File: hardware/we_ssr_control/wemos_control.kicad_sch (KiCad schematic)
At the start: 17 parts, among them U1 WeMos_D1_mini

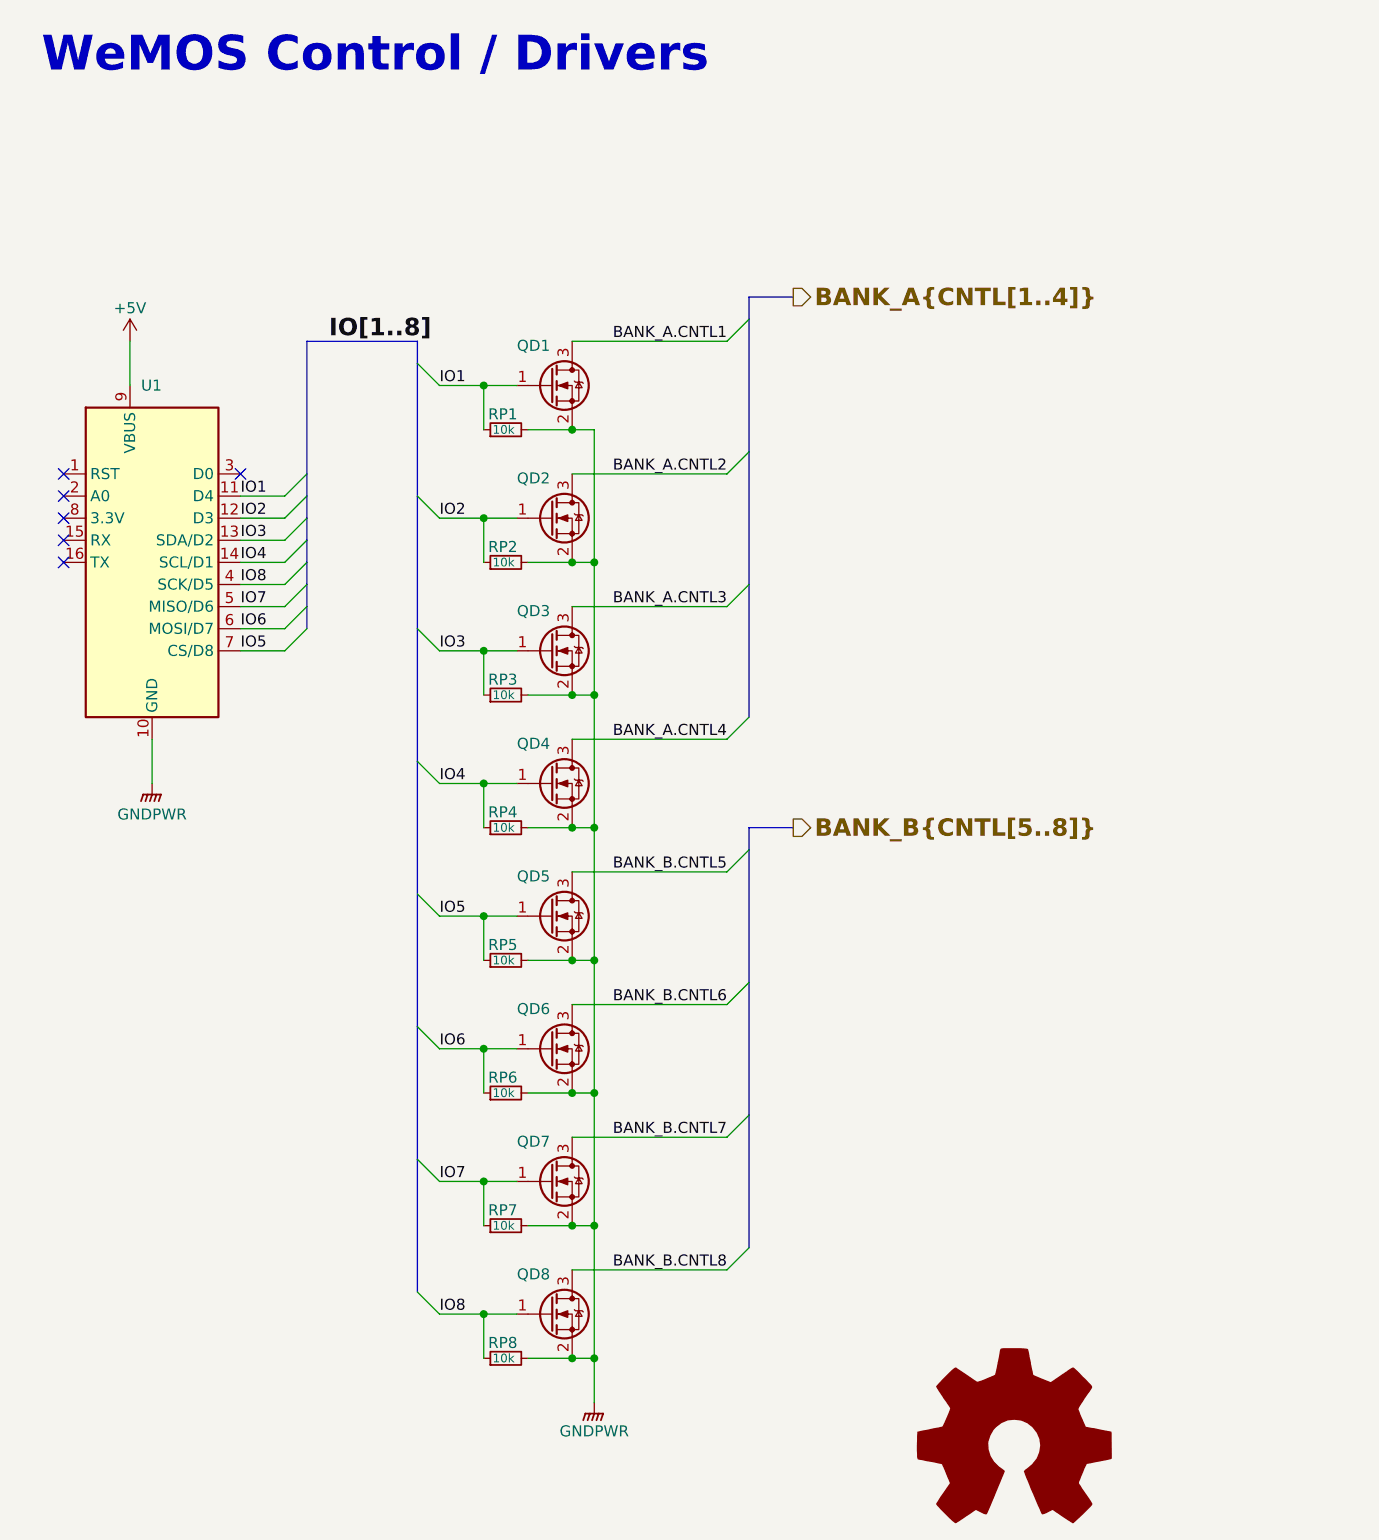
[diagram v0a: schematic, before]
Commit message: Power supply changes plus misc.
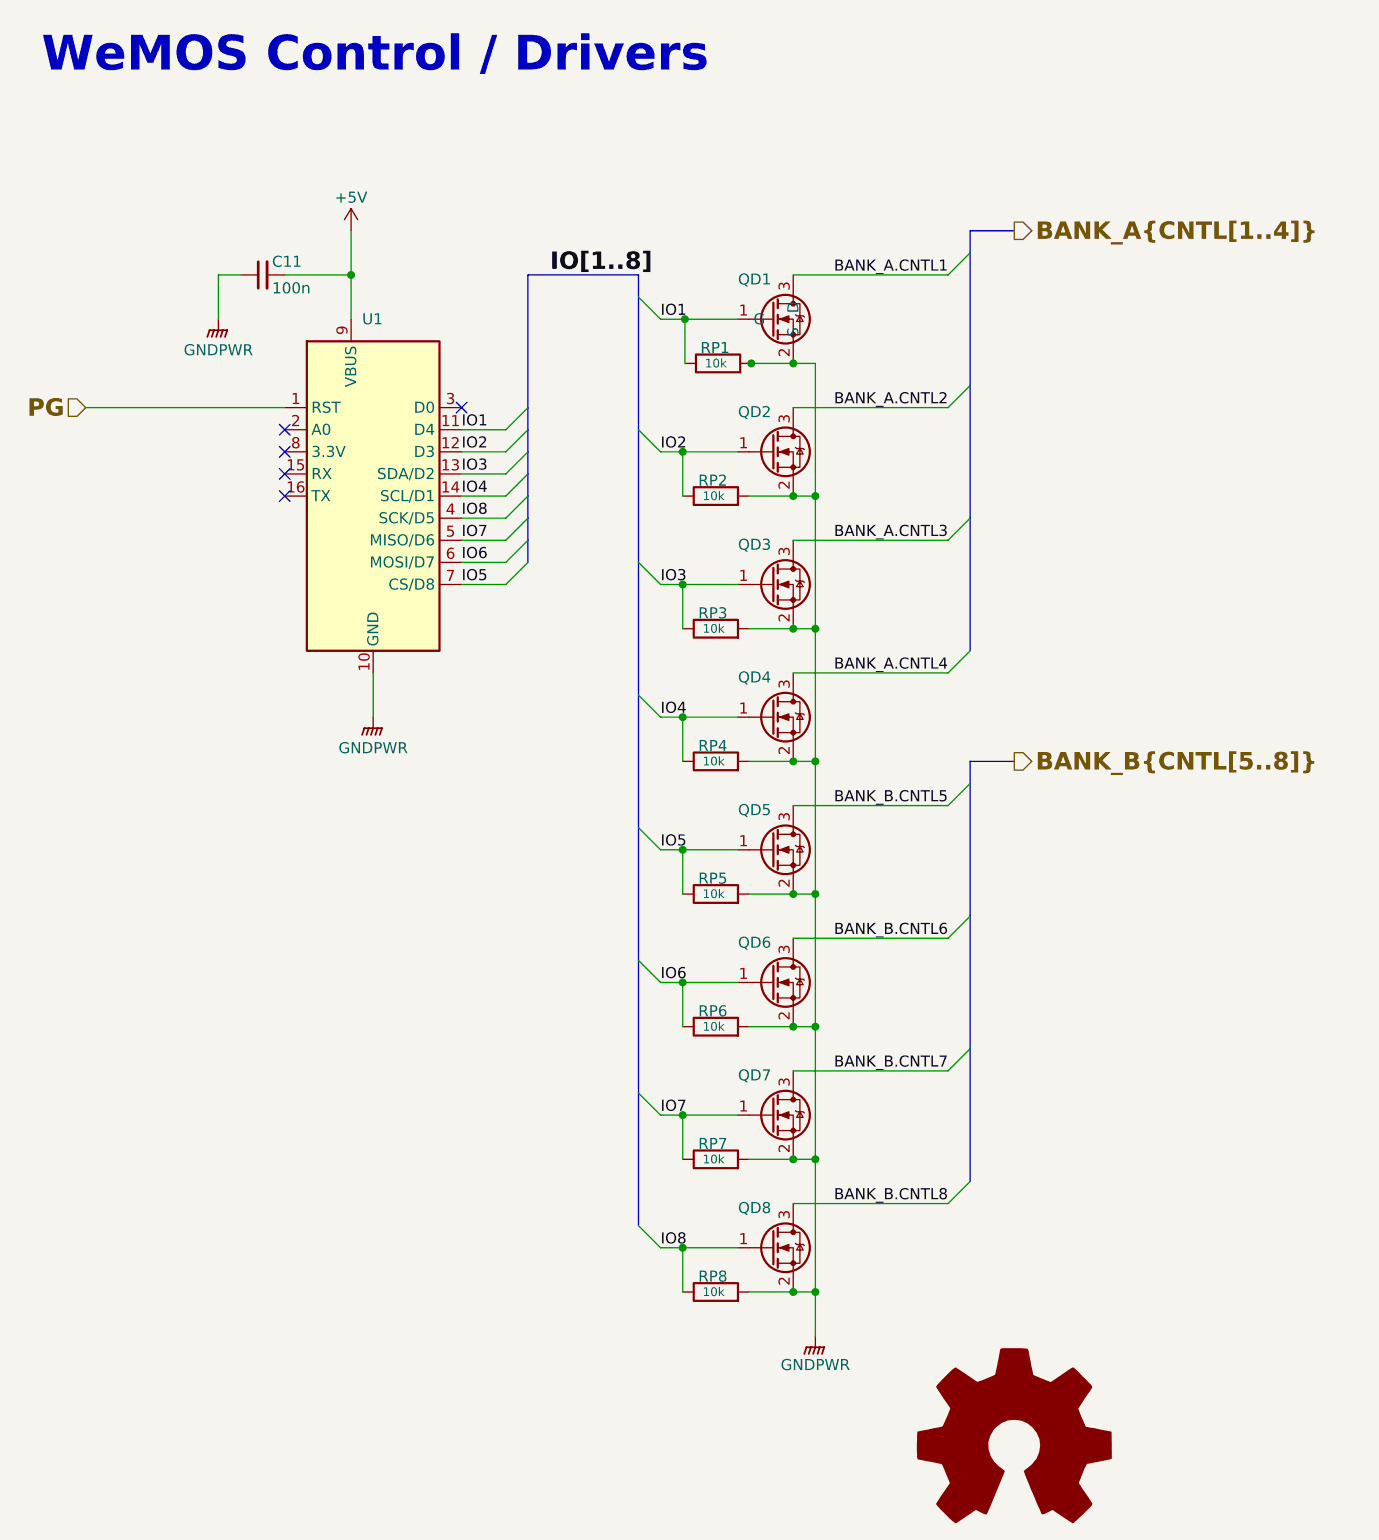
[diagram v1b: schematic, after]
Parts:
- added C11: 100n, Capacitor_SMD:C_0603_1608Metric, symbol Device:C_Small
- QD1, QD2, QD3, QD4, QD5, QD6, QD7, QD8: footprint Package_TO_SOT_SMD:SOT-23 -> Package_TO_SOT_SMD:SOT-23-3; Characteristics (none) -> MOSFET N Ch 60Vds, +- 20Vgs, 380mA, 2.5Ohms, 420mW, AEC-Q10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; Height (mm) (none) -> 1.10; MFN (none) -> onsemi; MFP (none) -> 2V7002KT1G; Mouser Part Number (none) -> 863-2V7002KT1G; Mouser Price/Stock (none) -> https://www.mouser.com/ProductDetail/onsemi/2V7002KT1G?qs=3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; Package (none) -> SOT-23-3; Type (none) -> SMD
- RP1, RP2, RP3, RP4, RP5, RP6, RP7, RP8: symbol Device:R_Small -> Device:R; Characteristics Thick Film Resistor - 10KΩ 5% 300mW; Anti Surge AEC-Q200; 1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 -> Thick Film Resistors - SMD 0603 10Kohm 5% Anti Surge AEC-Q2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
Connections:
- net +5V: now also C11.2
- net GNDPWR: now also C11.1
- net PG: now reaches U1.1 (RST)
- no-connect marks 6 -> 5
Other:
- moved on the sheet: QD2, QD3, QD4, QD5, QD6, QD7, QD8, RP1, RP2, RP3, RP4, RP5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

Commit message: Pre KiCad 7.0.0 WIP
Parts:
- QD1, QD2, QD3, QD4, QD5, QD6, QD7, QD8: footprint Package_TO_SOT_SMD:SOT-23-3 -> dragon_mobile:2V7002KT1G
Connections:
- net BANK_A.CNTL1 renamed BANK_A.OUT1
- net BANK_A.CNTL2 renamed BANK_A.OUT2
- net BANK_A.CNTL3 renamed BANK_A.OUT3
- net BANK_A.CNTL4 renamed BANK_A.OUT4
- net BANK_B.CNTL5 renamed BANK_B.OUT5
- net BANK_B.CNTL6 renamed BANK_B.OUT6
- net BANK_B.CNTL7 renamed BANK_B.OUT7
- net BANK_B.CNTL8 renamed BANK_B.OUT8
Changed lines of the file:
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@@
   (no_connect (at 43.18 66.04))
   (bus_entry (at 119.38 88.9) (size 2.54 -2.54)
-    (stroke (width 0) (type default) (color 0 0 0 0))
+    (stroke (width 0) (type default) (color 255 255 0 1))
   )
   (bus_entry (at 71.12 76.2) (size -2.54 2.54)
@@
   )
   (bus_entry (at 119.38 58.42) (size 2.54 -2.54)
-    (stroke (width 0) (type default) (color 0 0 0 0))
+    (stroke (width 0) (type default) (color 255 255 0 1))
   )
   (bus_entry (at 83.82 121.92) (size 2.54 2.54)
@@
   )
   (bus_entry (at 119.38 43.18) (size 2.54 -2.54)
-    (stroke (width 0) (type default) (color 0 0 0 0))
+    (stroke (width 0) (type default) (color 255 255 0 1))
   )
   (bus_entry (at 119.38 104.14) (size 2.54 -2.54)
-    (stroke (width 0) (type default) (color 0 0 0 0))
+    (stroke (width 0) (type default) (color 255 255 0 1))
   )
   (bus_entry (at 83.82 106.68) (size 2.54 2.54)
@@
   )
   (bus_entry (at 119.38 149.86) (size 2.54 -2.54)
-    (stroke (width 0) (type default) (color 0 0 0 0))
+    (stroke (width 0) (type default) (color 255 255 0 1))
   )
   (bus_entry (at 83.82 152.4) (size 2.54 2.54)
@@
   )
   (bus_entry (at 119.38 73.66) (size 2.54 -2.54)
-    (stroke (width 0) (type default) (color 0 0 0 0))
+    (stroke (width 0) (type default) (color 255 255 0 1))
   )
   (bus_entry (at 83.82 91.44) (size 2.54 2.54)
@@
   )
   (bus_entry (at 119.38 119.38) (size 2.54 -2.54)
-    (stroke (width 0) (type default) (color 0 0 0 0))
+    (stroke (width 0) (type default) (color 255 255 0 1))
   )
   (bus_entry (at 119.38 134.62) (size 2.54 -2.54)
-    (stroke (width 0) (type default) (color 0 0 0 0))
+    (stroke (width 0) (type default) (color 255 255 0 1))
   )
   (wire (pts (xy 43.18 43.18) (xy 50.8 43.18))
@@
     (effects (font (size 4 4) bold) (justify left bottom))
   )
-  (label "BANK_A.CNTL4" (at 119.38 88.9 180)
+  (label "BANK_A.OUT4" (at 119.38 88.9 180)
     (effects (font (size 1.27 1.27)) (justify right bottom))
   )
@@
     (effects (font (size 1.27 1.27)) (justify left bottom))
   )
-  (label "BANK_B.CNTL6" (at 119.38 119.38 180)
+  (label "BANK_B.OUT6" (at 119.38 119.38 180)
     (effects (font (size 1.27 1.27)) (justify right bottom))
   )
-  (label "BANK_B.CNTL5" (at 119.38 104.14 180)
+  (label "BANK_B.OUT5" (at 119.38 104.14 180)
     (effects (font (size 1.27 1.27)) (justify right bottom))
   )
@@
     (effects (font (size 1.27 1.27)) (justify left bottom))
   )
-  (label "BANK_B.CNTL7" (at 119.38 134.62 180)
+  (label "BANK_B.OUT7" (at 119.38 134.62 180)
     (effects (font (size 1.27 1.27)) (justify right bottom))
   )
@@
     (effects (font (size 1.27 1.27)) (justify left bottom))
   )
-  (label "BANK_A.CNTL1" (at 119.38 43.18 180)
+  (label "BANK_A.OUT1" (at 119.38 43.18 180)
     (effects (font (size 1.27 1.27)) (justify right bottom))
   )
@@
     (effects (font (size 1.27 1.27)) (justify left bottom))
   )
-  (label "BANK_A.CNTL3" (at 119.38 73.66 180)
+  (label "BANK_A.OUT3" (at 119.38 73.66 180)
     (effects (font (size 1.27 1.27)) (justify right bottom))
   )
-  (label "BANK_A.CNTL2" (at 119.38 58.42 180)
+  (label "BANK_A.OUT2" (at 119.38 58.42 180)
     (effects (font (size 1.27 1.27)) (justify right bottom))
   )
@@
     (effects (font (size 1.27 1.27)) (justify left bottom))
   )
-  (label "BANK_B.CNTL8" (at 119.38 149.86 180)
+  (label "BANK_B.OUT8" (at 119.38 149.86 180)
     (effects (font (size 1.27 1.27)) (justify right bottom))
   )
@@
     (effects (font (size 1.27 1.27)) (justify left bottom))
   )
-  (hierarchical_label "BANK_B{CNTL[5..8]}" (shape output) (at 127 99.06 0)
+  (hierarchical_label "BANK_B{OUT[5..8]}" (shape output) (at 127 99.06 0)
     (effects (font (size 2 2) (thickness 0.4) bold) (justify left))
   )
@@
     (effects (font (size 2 2) bold) (justify right))
   )
-  (hierarchical_label "BANK_A{CNTL[1..4]}" (shape output) (at 127 38.1 0)
+  (hierarchical_label "BANK_A{OUT[1..4]}" (shape output) (at 127 38.1 0)
     (effects (font (size 2 2) (thickness 0.4) bold) (justify left))
   )
@@
       (effects (font (size 1.27 1.27)) (justify left) hide)
     )
-    (property "Footprint" "Package_TO_SOT_SMD:SOT-23-3" (id 2) (at 105.41 67.945 0)
-      (effects (font (size 1.27 1.27) italic) (justify left) hide)
+    (property "Footprint" "dragon_mobile:2V7002KT1G" (id 2) (at 105.41 67.945 0)
+      (effects (font (size 1.27 1.27)) (justify left) hide)
     )
     (property "Datasheet" "https://www.mouser.com/datasheet/2/308/2N7002K_D-1571268.pdf" (id 3) (at 105.41 71.12 0)
@@
     )
     (property "Characteristics" "MOSFET N Ch 60Vds, +- 20Vgs, 380mA, 2.5Ohms, 420mW, AEC-Q101 SMD (0603)" (id 4) (at 99.06 48.26 0)
-      (effects (font (size 1.27 1.27)) hide)
+      (effects (font (size 1.27 1.27)) (justify left) hide)
     )
     (property "Description" "MOSFET N Ch 60Vds, +- 20Vgs, 380mA, 2.5Ohms, 420mW, AEC-Q101 SMD (0603)" (id 5) (at 99.06 48.26 0)
-      (effects (font (size 1.27 1.27)) hide)
+      (effects (font (size 1.27 1.27)) (justify left) hide)
     )
     (property "Height (mm)" "1.10" (id 6) (at 99.06 48.26 0)
-      (effects (font (size 1.27 1.27)) hide)
+      (effects (font (size 1.27 1.27)) (justify left) hide)
     )
     (property "MFN" "onsemi" (id 7) (at 99.06 48.26 0)
-      (effects (font (size 1.27 1.27)) hide)
+      (effects (font (size 1.27 1.27)) (justify left) hide)
     )
     (property "MFP" "2V7002KT1G" (id 8) (at 99.06 48.26 0)
-      (effects (font (size 1.27 1.27)) hide)
+      (effects (font (size 1.27 1.27)) (justify left) hide)
     )
     (property "Mouser Part Number" "863-2V7002KT1G" (id 9) (at 99.06 48.26 0)
-      (effects (font (size 1.27 1.27)) hide)
+      (effects (font (size 1.27 1.27)) (justify left) hide)
     )
     (property "Mouser Price/Stock" "https://www.mouser.com/ProductDetail/onsemi/2V7002KT1G?qs=3PKVEWFFm2%252BHUKlmW8gbSQ%3D%3D" (id 10) (at 99.06 48.26 0)
-      (effects (font (size 1.27 1.27)) hide)
+      (effects (font (size 1.27 1.27)) (justify left) hide)
     )
     (property "Package" "SOT-23-3" (id 11) (at 99.06 48.26 0)
-      (effects (font (size 1.27 1.27)) hide)
+      (effects (font (size 1.27 1.27)) (justify left) hide)
     )
     (property "Type" "SMD" (id 12) (at 99.06 48.26 0)
-      (effects (font (size 1.27 1.27)) hide)
+      (effects (font (size 1.27 1.27)) (justify left) hide)
     )
     (pin "1")
@@
       (effects (font (size 1.27 1.27)) (justify left) hide)
     )
-    (property "Footprint" "Package_TO_SOT_SMD:SOT-23-3" (id 2) (at 105.41 113.665 0)
+    (property "Footprint" "dragon_mobile:2V7002KT1G" (id 2) (at 105.41 113.665 0)
       (effects (font (size 1.27 1.27) italic) (justify left) hide)
     )
@@
       (effects (font (size 1.27 1.27)) (justify left) hide)
     )
-    (property "Footprint" "Package_TO_SOT_SMD:SOT-23-3" (id 2) (at 105.41 128.905 0)
+    (property "Footprint" "dragon_mobile:2V7002KT1G" (id 2) (at 105.41 128.905 0)
       (effects (font (size 1.27 1.27) italic) (justify left) hide)
     )
@@
       (effects (font (size 1.27 1.27)) (justify left) hide)
     )
-    (property "Footprint" "Package_TO_SOT_SMD:SOT-23-3" (id 2) (at 105.41 98.425 0)
+    (property "Footprint" "dragon_mobile:2V7002KT1G" (id 2) (at 105.41 98.425 0)
       (effects (font (size 1.27 1.27) italic) (justify left) hide)
     )
@@
       (effects (font (size 1.27 1.27)) (justify left) hide)
     )
-    (property "Footprint" "Package_TO_SOT_SMD:SOT-23-3" (id 2) (at 105.41 174.625 0)
+    (property "Footprint" "dragon_mobile:2V7002KT1G" (id 2) (at 105.41 174.625 0)
       (effects (font (size 1.27 1.27) italic) (justify left) hide)
     )
@@
       (effects (font (size 1.27 1.27)) (justify left) hide)
     )
-    (property "Footprint" "Package_TO_SOT_SMD:SOT-23-3" (id 2) (at 105.41 144.145 0)
+    (property "Footprint" "dragon_mobile:2V7002KT1G" (id 2) (at 105.41 144.145 0)
       (effects (font (size 1.27 1.27) italic) (justify left) hide)
     )
@@
       (effects (font (size 1.27 1.27)) (justify left) hide)
     )
-    (property "Footprint" "Package_TO_SOT_SMD:SOT-23-3" (id 2) (at 105.41 83.185 0)
+    (property "Footprint" "dragon_mobile:2V7002KT1G" (id 2) (at 105.41 83.185 0)
       (effects (font (size 1.27 1.27) italic) (justify left) hide)
     )
@@
       (effects (font (size 1.27 1.27)) (justify left) hide)
     )
-    (property "Footprint" "Package_TO_SOT_SMD:SOT-23-3" (id 2) (at 105.41 159.385 0)
+    (property "Footprint" "dragon_mobile:2V7002KT1G" (id 2) (at 105.41 159.385 0)
       (effects (font (size 1.27 1.27) italic) (justify left) hide)
     )
